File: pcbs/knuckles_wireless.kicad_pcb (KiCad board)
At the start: 2 copper layers, 137.3 x 113.5 mm, 120 parts

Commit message: feat: prepare wireless board for TPS43 and validate autorouting
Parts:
- removed DISP1: , ceoloide:display_nice_view
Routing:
- net SDA: track 3.50 -> 0.00 mm
- net SCL: track 3.50 -> 0.00 mm
- net GND: track 3.50 -> 0.00 mm
- net CS: track 3.50 -> 0.00 mm

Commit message: feat: add Knuckles logo and reversible PCB silkscreen
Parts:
- added ART1: , knuckles_artwork_badge, F.Cu at (217.5, 105.4)
- added ART2: , knuckles_artwork_wordmark, F.Cu at (140.0, 105.8)
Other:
- board text added: "v1.0"
- board text removed: "knuckles v1.0"

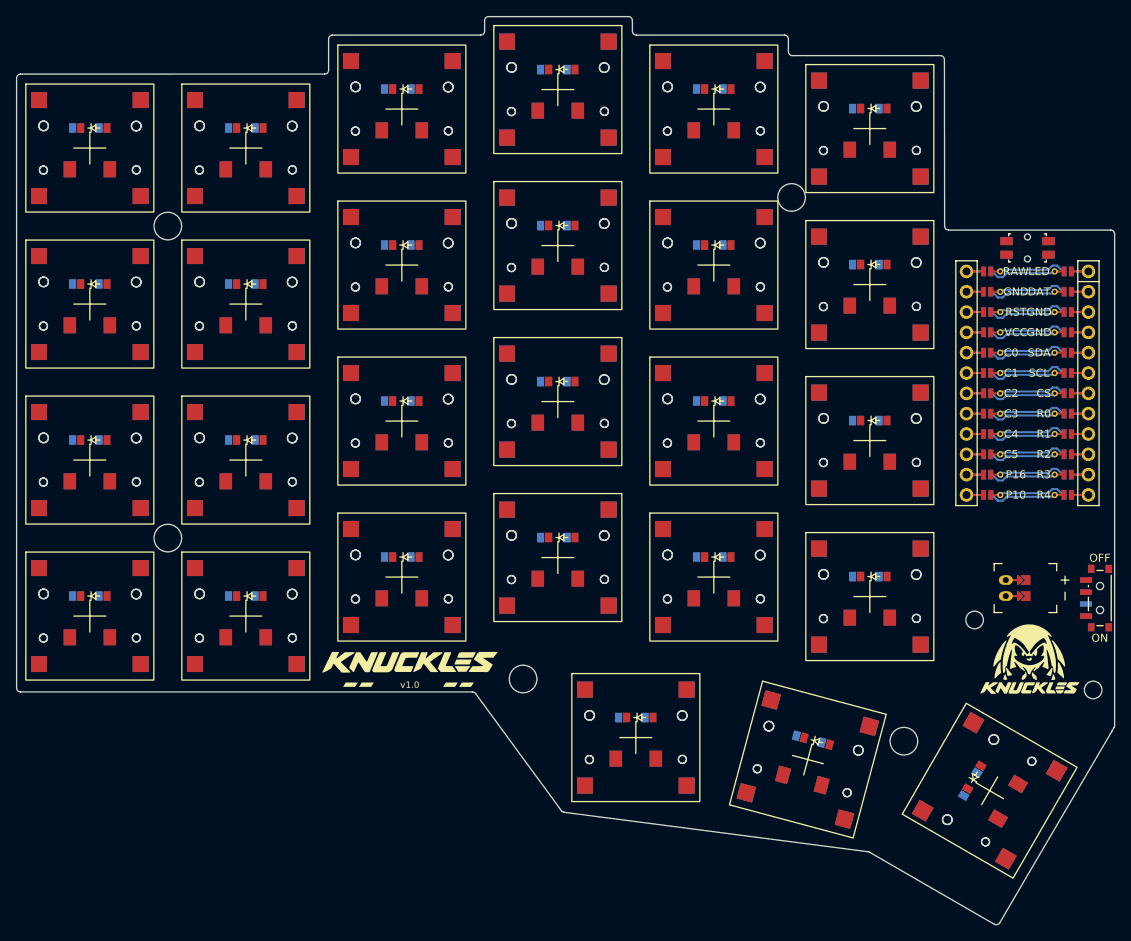
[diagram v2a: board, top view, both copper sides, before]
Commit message: feat: default to compact 18.5 mm layout and refresh generated boards
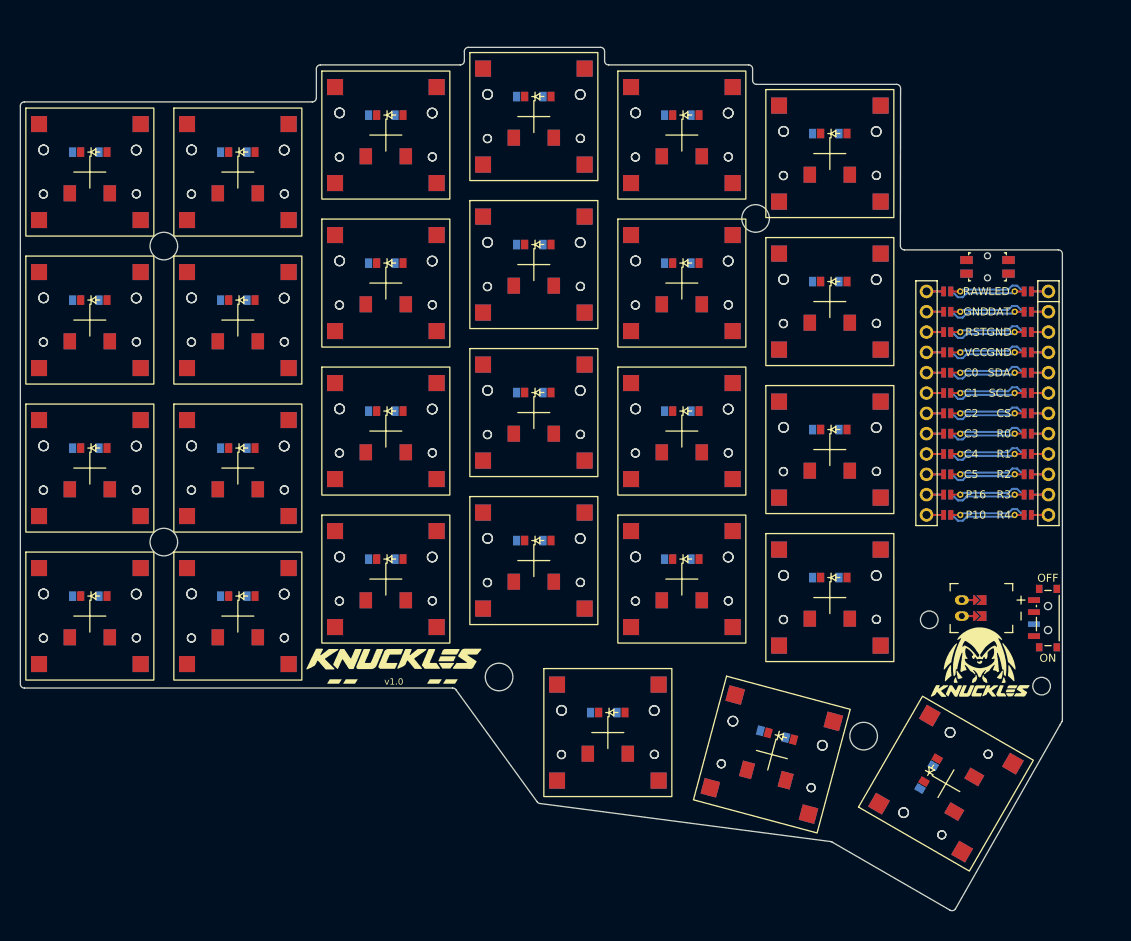
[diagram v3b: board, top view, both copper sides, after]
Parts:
- moved PWR1 6.96 mm to (219.8, 100.2)
- moved MH2 6.47 mm to (219.0, 108.8)
- moved ART1 6.21 mm to (211.3, 105.8)
- moved JST1 6.04 mm to (209.0, 99.0)
- moved D24 5.90 mm to (192.0, 39.7)
- moved D51 5.90 mm to (193.0, 39.7)
- moved S24 5.90 mm to (192.5, 42.2)
- moved S51 5.90 mm to (192.5, 42.2)
- moved MH1 5.67 mm to (204.9, 100.5)
- moved MCU1 5.59 mm to (212.2, 72.1)
- moved D27 5.54 mm to (204.6, 120.1)
- moved D54 5.54 mm to (205.1, 119.3)
- moved S27 5.54 mm to (207.0, 120.9)
- moved S54 5.54 mm to (207.0, 120.9)
- moved RST1 5.53 mm to (212.2, 56.3)
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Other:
- board size 137.3 x 113.5 mm -> 130.3 x 107.9 mm

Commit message: Archive ordered wireless PCB and manufacturing files
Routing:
- net (no net): track 333.1 -> 0.00 mm
- net GND: track 0.00 -> 28.9 mm
- net C3: track 0.00 -> 9.64 mm
- net C1: track 0.00 -> 9.64 mm
- net VCC: track 0.00 -> 9.64 mm
- net RST: track 0.00 -> 9.64 mm
- net RAW: track 0.00 -> 9.64 mm
- net P16: track 0.00 -> 9.64 mm
- net P10: track 0.00 -> 9.64 mm
- net C5: track 0.00 -> 9.64 mm
- net C4: track 0.00 -> 9.64 mm
- net C2: track 0.00 -> 9.64 mm
- net C0: track 0.00 -> 9.64 mm
- net SDA: track 0.00 -> 9.63 mm
- net R3: track 0.00 -> 9.63 mm
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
